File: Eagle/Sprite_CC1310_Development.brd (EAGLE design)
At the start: 50 x 50 mm, 68 parts

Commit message: Fixed HDMI
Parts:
- removed U$1: HDMID, HDMID:HDMID
- added R14, R16: 0, SparkFun:0603-RES
- added U$9: HDMID, HDMID:HDMID
- moved L3 3.45 mm to (31.7, 4.99), turned to 180 degrees
- moved R15 3.02 mm to (30.5, 7.67), turned to 90 degrees
- moved C23 0.71 mm to (44.8, 22.9), turned to 270 degrees
- moved R21 0.27 mm to (21.8, 19.3)
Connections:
- new net N$16: R16.2, U$7.SIG
- new net N$40: R14.1, U$3.SIG
- net GND: now also U$9.1, U$9.FOOT1, U$9.FOOT2, U$9.FOOT3, U$9.FOOT4; no longer U$1.19, U$1.FOOT1, U$1.FOOT2, U$1.FOOT3, U$1.FOOT4
- net JTAG_TCKC: now also U$9.14, U$9.15; no longer U$1.5, U$1.6
- net JTAG_TMSC: now also U$9.16, U$9.17; no longer U$1.3, U$1.4
- net N$14: now also R16.1; no longer U$7.SIG
- net N$26: now also R14.2; no longer U$3.SIG
- net RESET: now also U$9.6, U$9.7; no longer U$1.13, U$1.14
- net RXD: now also U$9.2, U$9.3; no longer U$1.17, U$1.18
- net SWO: now also U$9.8, U$9.9; no longer U$1.11, U$1.12
- net TDI: now also U$9.10, U$9.11; no longer U$1.10, U$1.9
- net TDO: now also U$9.12, U$9.13; no longer U$1.7, U$1.8
- net TXD: now also U$9.4, U$9.5; no longer U$1.15, U$1.16
- net VDDS: now also U$9.18, U$9.19; no longer U$1.1, U$1.2
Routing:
- net VDDS: track 124.6 -> 118.5 mm
- net GND: track 210.1 -> 204.6 mm, vias 13 -> 12
- net SWO: track 16.7 -> 12.6 mm
- net JTAG_TCKC: track 16.7 -> 12.8 mm
- net RESET: track 16.3 -> 12.4 mm
- net TDO: track 16.7 -> 12.7 mm
- net JTAG_TMSC: track 17.4 -> 13.4 mm
- net TDI: track 16.6 -> 12.7 mm
- net TXD: track 41.9 -> 38.2 mm
- net RXD: track 49.7 -> 46.0 mm
- net N$40: track 0.00 -> 3.35 mm
- net N$15: track 15.6 -> 12.8 mm
- net N$16: track 0.00 -> 2.21 mm
- net N$26: track 8.69 -> 7.47 mm

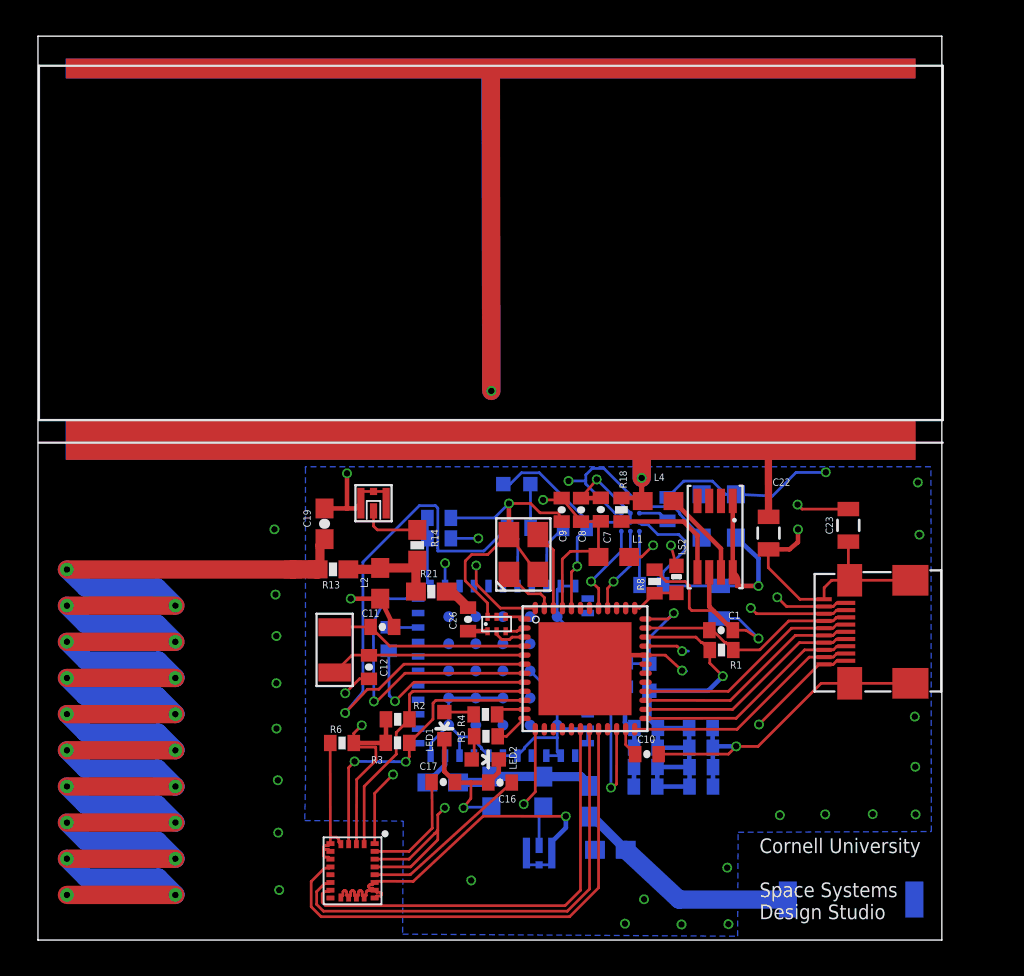
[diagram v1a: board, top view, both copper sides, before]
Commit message: updated boost converter, eliminated unnecessary tuning components, rotated oscillator, updated solar pads
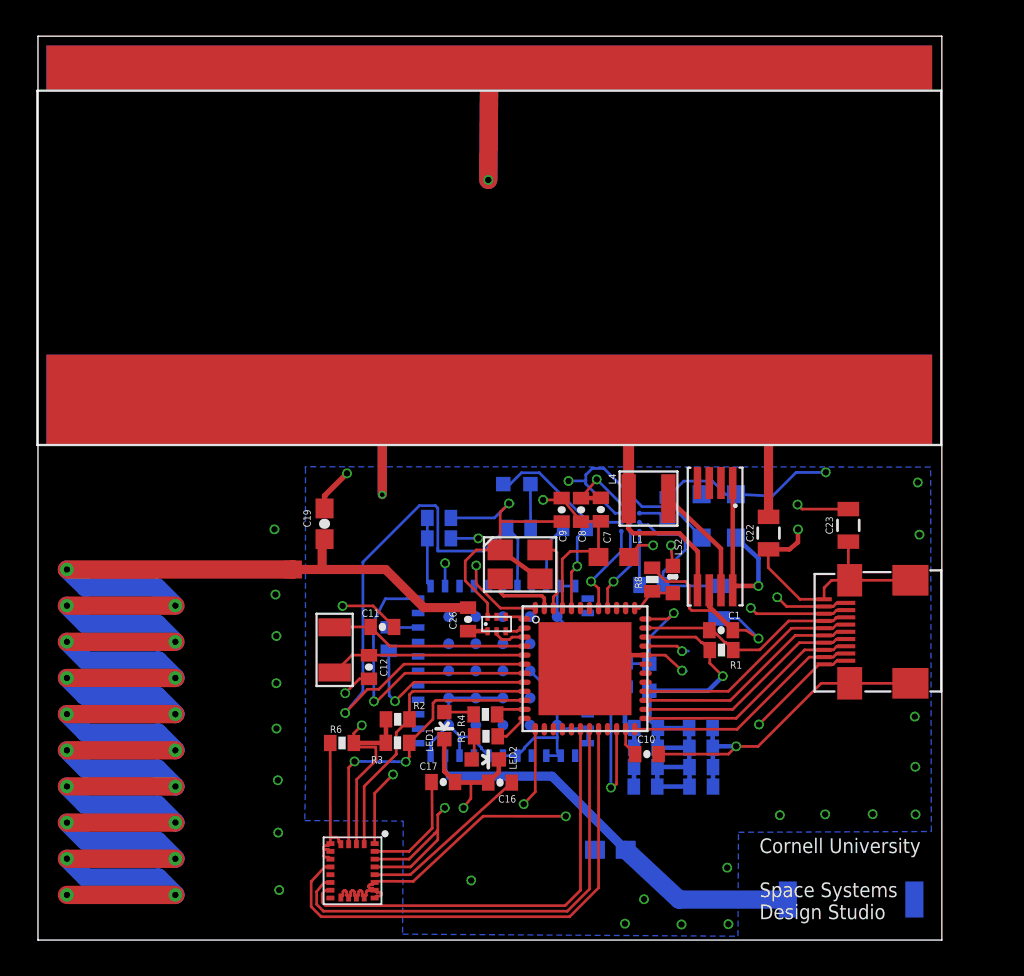
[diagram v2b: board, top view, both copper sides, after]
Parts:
- removed L2: DNP, SparkFun:0603
- removed R13, R14, R15, R16, R21, R22: 0, SparkFun:0603-RES
- removed R17: DNP, SparkFun:0603-RES
- removed R18: 10k, SparkFun:0402-RES
- removed U$3, U$7: MM5329-2700, MM5329-2700:MM5829-2700
- L4: value 47uH -> 10uH; device SparkFun:0603 -> ASPI-0315FS:ASPI-0315FS
- moved FRONT_PANEL 1.39 mm to (25.0, 37.2)
- moved REAR_PANEL 1.38 mm to (25.0, 37.2)
- moved TSX3225 0.58 mm to (26.7, 20.8), turned to 0 degrees
- moved L4 0.55 mm to (33.8, 24.4)
- moved LS2 0.20 mm to (35.1, 19.9)
- moved R8 0.17 mm to (34.0, 19.9)
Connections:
- removed net N$14: R15.2, R16.1, R17.1, R22.1
- removed net N$16: R16.2, U$7.SIG
- removed net N$25: GPS.32, R22.2
- removed net N$26: L2.1, R13.1, R14.2, R21.2
- removed net N$27: C26.1, R21.1
- removed net N$40: R14.1, U$3.SIG
- removed net N$41: R18.1, U$8.5
- net ANTENNA: now also C26.1; no longer R13.2
- net GND: no longer L2.2, R17.2, U$3.GND1, U$3.GND2, U$3.GND3, U$7.GND1, U$7.GND2, U$7.GND3
- net N$15: now also GPS.32; no longer R15.1
- net SOLAR_CELLS: now also U$8.5; no longer R18.2
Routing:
- net GND: track 204.6 -> 181.2 mm
- net SOLAR_CELLS: track 35.4 -> 50.1 mm
- net N$15: track 12.8 -> 22.7 mm
- net ANTENNA: track 131.2 -> 140.3 mm
- net N$14: track 7.66 -> 0.00 mm
- net N$26: track 7.47 -> 0.00 mm
- net N$41: track 6.57 -> 0.00 mm
- net N$40: track 3.35 -> 0.00 mm
- net N$16: track 2.21 -> 0.00 mm
- net N$25: track 1.89 -> 0.00 mm
- net N$27: track 1.55 -> 0.00 mm
- net VDDS: track 118.5 -> 120.0 mm
- net N$48: track 5.03 -> 6.32 mm
- net X24M_P: track 3.08 -> 3.87 mm

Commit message: still need to add breakouts
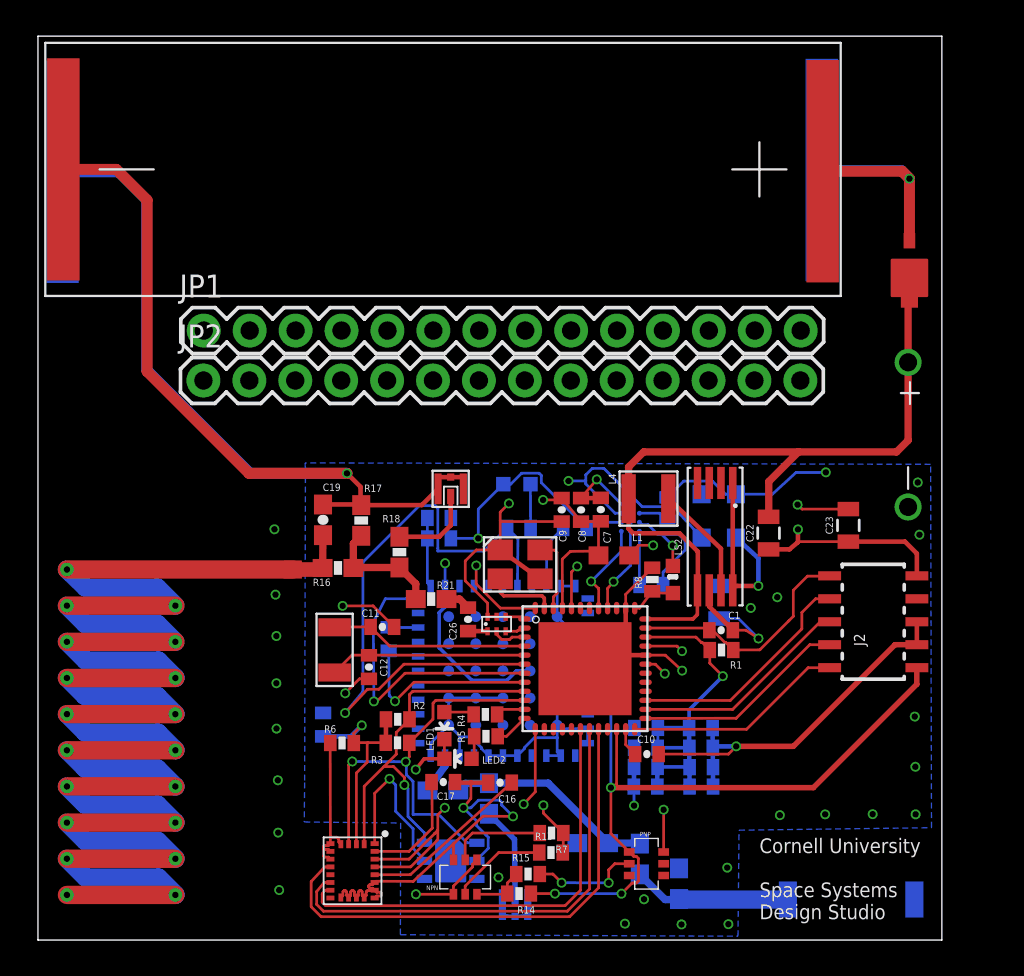
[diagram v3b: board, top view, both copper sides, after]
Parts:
- removed LS1: LIGHTSENSORALS, SparkFun-Sensors:ALS-PT19
- removed U$9: HDMID, HDMID:HDMID
- added C21: 0.1 uF, SparkFun:0402-CAP
- added J2: CORTEX_DEBUG_SMD, SparkFun-Connectors:SAMTECH_FTSH-105-01
- added JP1, JP2: (no value), SparkFun-Connectors:1X14
- added NPN: MMDT3904, mmdt3904:MMDT3904
- added PNP: MMDT3906, mmdt3906:MMDT3906
- added R13, R15: 330, SparkFun:0402-RES
- added R14: 10k, SparkFun:0402-RES
- added R16, R21, R22, R23: 0, SparkFun:0603-RES
- added R17, R18, R24, R25: DNP, SparkFun:0603-RES
- added SCHTOKKY: STPS1L30MF, stps1l30mf:STPS1L30MF
- added SI7021: SI7021, si7021:SI7021
- added SUPERCAPACITOR: SUPERCAP1, supercap1:SUPERCAP1
- added U$1, U$3: MM5329-2700, MM5329-2700:MM5829-2700
- FRONT_PANEL, REAR_PANEL: value ALTA_CELL -> SOLARMD; device ALTA_CELL:ALTA_CELL -> solarmd:SOLARMD
- R20: value 331 -> 330
- R7: value 10k -> 330
- moved R7 9.64 mm to (28.4, 5.92), flipped to the top, turned to 180 degrees
- moved FRONT_PANEL 6.02 mm to (22.4, 42.6), flipped to the top, turned to 0 degrees
- moved REAR_PANEL 5.92 mm to (22.4, 42.5), flipped to the bottom
- moved L3 4.24 mm to (35.5, 3.12), turned to 270 degrees
- moved LED2 1.51 mm to (23.2, 10.0), turned to 90 degrees
- moved C19 0.24 mm to (15.8, 23.2)
- moved L1 0.09 mm to (31.9, 21.3)
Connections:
- removed net ADC0: LS1.E, MICROCONTROLLER.36, R7.1
- new net BPNP: NPN.6, R14.2, R15.1
- new net IMUGND: C13.2, C14.2, C15.2, C16.2, C17.2, IMU.14, IMU.15, IMU.16, IMU.17, IMU.18, IMU.19, IMU.20, NPN.3, SI7021.2
- new net N$14: NPN.2, R7.2
- new net N$16: NPN.5, R13.1
- new net N$25: PNP.2, R15.2
- new net N$26: R16.2, R17.1, R18.2, R21.1
- new net N$27: C26.1, R21.2
- new net N$40: R18.1, U$1.SIG
- new net N$41: GPS.32, R22.1
- new net N$49: R22.2, R23.1, R24.1, R25.1
- new net N$50: R25.2, U$3.SIG
- new net SUPERCAP: C22.1, L4.2, MICROCONTROLLER.36, SCHTOKKY.-, SUPERCAPACITOR.+, U$8.5
- new net TRANS: MICROCONTROLLER.31, R13.2, R7.1
- new net VSENSE: GPS.2, GPS.58, LED3.A, LS2.C, PNP.6, R11.2, R12.1, R19.2, U$2.VCC, U$2.VM
- net ANTENNA: now also R16.1; no longer C26.1
- net GND: now also C21.2, J2.3, J2.5, J2.9, MICROCONTROLLER.38, NPN.1, NPN.4, R17.2, R24.2, SUPERCAPACITOR.-, U$1.GND1, U$1.GND2, U$1.GND3, U$3.GND1, U$3.GND2, U$3.GND3; no longer C13.2, C14.2, C15.2, C16.2, C17.2, IMU.14, IMU.15, IMU.16, IMU.17, IMU.18, IMU.19, IMU.20, R7.2, U$9.1, U$9.FOOT1, U$9.FOOT2, U$9.FOOT3, U$9.FOOT4
- net JTAG_TCKC: now also J2.4; no longer U$9.14, U$9.15
- net JTAG_TMSC: now also J2.2; no longer U$9.16, U$9.17
- net N$15: now also R23.2; no longer GPS.32
- net RESET: now also J2.10; no longer U$9.6, U$9.7
- net RXD: no longer U$9.2, U$9.3
- net SCL: now also SI7021.6
- net SDA: now also SI7021.1
- net SOLAR_CELLS: now also SCHTOKKY.+; no longer C22.1, L4.2, U$8.5
- net SWO: no longer U$9.8, U$9.9
- net TDI: now also J2.8; no longer U$9.10, U$9.11
- net TDO: now also J2.6; no longer U$9.12, U$9.13
- net TXD: no longer U$9.4, U$9.5
- net VDDS: now also C21.1, J2.1, PNP.1, R14.1, SI7021.5; no longer GPS.2, GPS.58, LED3.A, LS1.C, LS2.C, R11.2, R12.1, R19.2, U$2.VCC, U$2.VM, U$9.18, U$9.19
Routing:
- net VSENSE: track 0.00 -> 64.3 mm, vias 0 -> 4
- net SUPERCAP: track 0.00 -> 42.3 mm
- net IMUGND: track 0.00 -> 37.0 mm, vias 0 -> 3
- net SOLAR_CELLS: track 50.1 -> 13.5 mm
- net TRANS: track 0.00 -> 14.6 mm, vias 0 -> 2
- net N$15: track 22.7 -> 8.79 mm
- net SWO: track 12.6 -> 0.00 mm
- net N$49: track 0.00 -> 11.6 mm
- net ANTENNA: track 140.3 -> 131.5 mm
- net SDA: track 16.6 -> 23.8 mm
- net ADC0: track 6.77 -> 0.00 mm, vias 1 -> 0
- net N$26: track 0.00 -> 6.64 mm
- net N$25: track 0.00 -> 6.01 mm, vias 0 -> 2
- net GND: track 181.2 -> 187.2 mm, vias 12 -> 11
- net TXD: track 38.2 -> 32.7 mm
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
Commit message: board layout complete, need to update other files
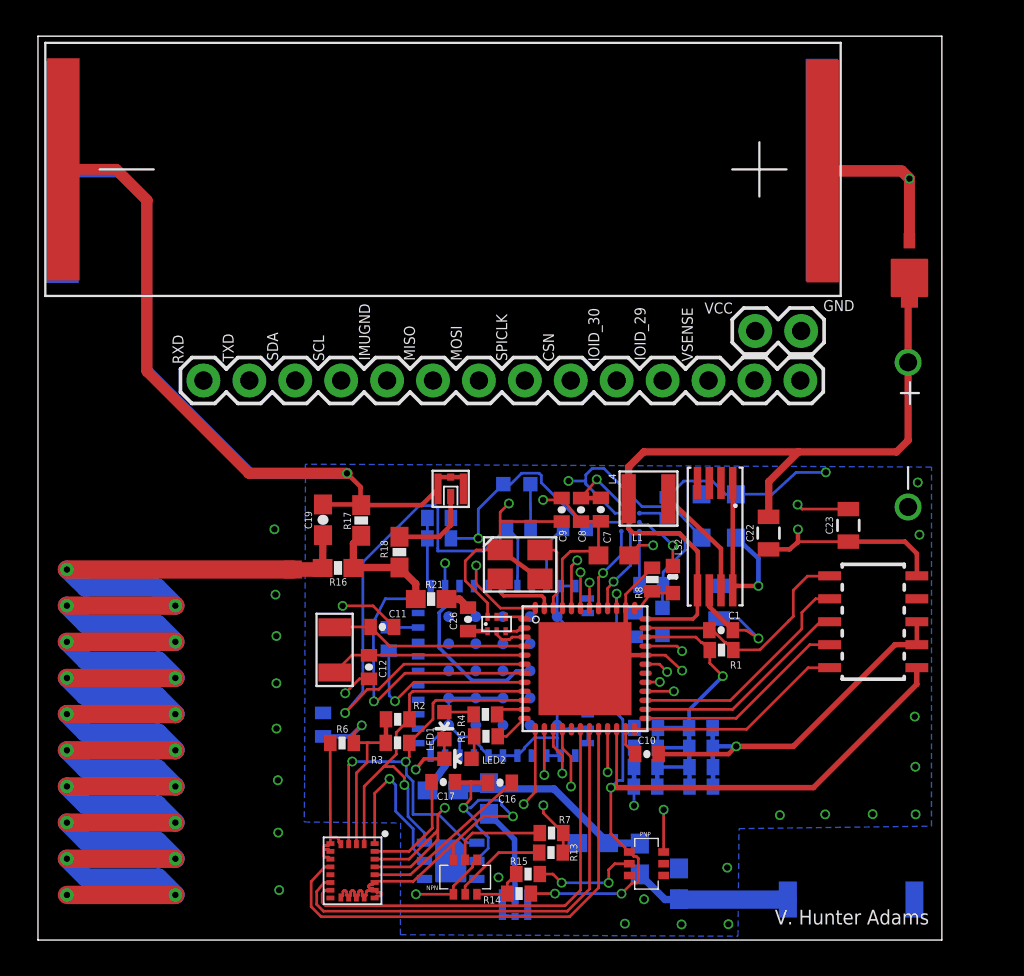
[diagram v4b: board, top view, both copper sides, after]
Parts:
- added LS1: LIGHTSENSORALS, SparkFun-Sensors:ALS-PT19
- added R26: 10k, SparkFun:0402-RES
- JP1: device SparkFun-Connectors:1X14 -> SparkFun:1X02
- moved JP1 30.5 mm to (39.7, 33.7)
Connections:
- removed net SWO: MICROCONTROLLER.28
- new net ADC2: LS1.E, MICROCONTROLLER.39, R26.1
- new net CSN: JP2.9, MICROCONTROLLER.21
- new net CTS: JP2.13, MICROCONTROLLER.29
- new net DIO_29: JP2.11, MICROCONTROLLER.42
- new net DIO_30: JP2.10, MICROCONTROLLER.43
- new net MISO: JP2.6, MICROCONTROLLER.14
- new net MOSI: JP2.7, MICROCONTROLLER.15
- new net RTS: JP2.14, MICROCONTROLLER.28
- new net SPICLK: JP2.8, MICROCONTROLLER.16
- net GND: now also JP1.2, R26.2
- net IMUGND: now also JP2.5
- net RXD: now also JP2.1
- net SCL: now also JP2.4
- net SDA: now also JP2.3
- net TXD: now also JP2.2
- net VDDS: now also JP1.1
- net VSENSE: now also JP2.12, LS1.C
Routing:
- net MOSI: track 0.00 -> 27.2 mm, vias 0 -> 1
- net MISO: track 0.00 -> 27.0 mm, vias 0 -> 1
- net SPICLK: track 0.00 -> 26.9 mm, vias 0 -> 1
- net CSN: track 0.00 -> 25.4 mm, vias 0 -> 1
- net IMUGND: track 37.0 -> 62.4 mm
- net SCL: track 21.2 -> 46.2 mm
- net SDA: track 23.8 -> 47.5 mm
- net RTS: track 0.00 -> 21.7 mm, vias 0 -> 1
- net CTS: track 0.00 -> 20.3 mm, vias 0 -> 1
- net DIO_29: track 0.00 -> 14.4 mm, vias 0 -> 1
- net DIO_30: track 0.00 -> 13.6 mm, vias 0 -> 1
- net VSENSE: track 64.3 -> 75.5 mm
- net ADC2: track 0.00 -> 5.66 mm, vias 0 -> 1
- net TRANS: track 14.6 -> 18.3 mm
- net RXD: track 41.9 -> 38.6 mm, vias 2 -> 1
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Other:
- board text added: "CSN"
- board text added: "GND"
- board text added: "IMUGND"
- board text added: "IOID_29"
- board text added: "IOID_30"
- board text added: "MISO"
- board text added: "MOSI"
- board text added: "RXD"
- board text added: "SCL"
- board text added: "SDA"
- board text added: "SPICLK"
- board text added: "TXD"
- board text added: "V. Hunter Adams"
- board text added: "VCC"
- board text added: "VSENSE"
- board text removed: "Cornell University Space Systems Design Studio"
- board text removed: "V. Hunter Adams VHA3@CORNELL.EDU"

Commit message: updated all files
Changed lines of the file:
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@@
 <setting verticaltext="up"/>
 </settings>
-<grid distance="0.002" unitdist="inch" unit="inch" style="lines" multiple="1" display="yes" altdistance="0.000123031496" altunitdist="mil" altunit="mil"/>
+<grid distance="0.002" unitdist="inch" unit="mm" style="lines" multiple="1" display="yes" altdistance="0.000003125" altunitdist="mm" altunit="mm"/>
 <layers>
-<layer number="1" name="Top" color="4" fill="1" visible="no" active="yes"/>
-<layer number="2" name="Route2" color="1" fill="3" visible="no" active="yes"/>
+<layer number="1" name="Top" color="4" fill="1" visible="yes" active="yes"/>
+<layer number="2" name="Route2" color="1" fill="3" visible="yes" active="yes"/>
 <layer number="3" name="Route3" color="4" fill="3" visible="no" active="yes"/>
 <layer number="4" name="Route4" color="1" fill="4" visible="no" active="yes"/>
@@
 <layer number="13" name="Route13" color="4" fill="5" visible="no" active="yes"/>
 <layer number="14" name="Route14" color="1" fill="6" visible="no" active="yes"/>
-<layer number="15" name="Route15" color="4" fill="6" visible="no" active="yes"/>
-<layer number="16" name="Bottom" color="1" fill="1" visible="yes" active="yes"/>
+<layer number="15" name="Route15" color="4" fill="6" visible="yes" active="yes"/>
+<layer number="16" name="Bottom" color="1" fill="1" visible="no" active="yes"/>
 <layer number="17" name="Pads" color="2" fill="1" visible="yes" active="yes"/>
 <layer number="18" name="Vias" color="2" fill="1" visible="yes" active="yes"/>
 <layer number="19" name="Unrouted" color="6" fill="1" visible="yes" active="yes"/>
 <layer number="20" name="Dimension" color="24" fill="1" visible="yes" active="yes"/>
-<layer number="21" name="tPlace" color="7" fill="1" visible="no" active="yes"/>
-<layer number="22" name="bPlace" color="7" fill="1" visible="yes" active="yes"/>
-<layer number="23" name="tOrigins" color="15" fill="1" visible="no" active="yes"/>
-<layer number="24" name="bOrigins" color="15" fill="1" visible="yes" active="yes"/>
-<layer number="25" name="tNames" color="7" fill="1" visible="no" active="yes"/>
-<layer number="26" name="bNames" color="7" fill="1" visible="yes" active="yes"/>
+<layer number="21" name="tPlace" color="7" fill="1" visible="yes" active="yes"/>
+<layer number="22" name="bPlace" color="7" fill="1" visible="no" active="yes"/>
+<layer number="23" name="tOrigins" color="15" fill="1" visible="yes" active="yes"/>
+<layer number="24" name="bOrigins" color="15" fill="1" visible="no" active="yes"/>
+<layer number="25" name="tNames" color="7" fill="1" visible="yes" active="yes"/>
+<layer number="26" name="bNames" color="7" fill="1" visible="no" active="yes"/>
 <layer number="27" name="tValues" color="7" fill="1" visible="no" active="yes"/>
-<layer number="28" name="bValues" color="7" fill="1" visible="yes" active="yes"/>
+<layer number="28" name="bValues" color="7" fill="1" visible="no" active="yes"/>
 <layer number="29" name="tStop" color="7" fill="3" visible="no" active="yes"/>
 <layer number="30" name="bStop" color="7" fill="6" visible="no" active="yes"/>
@@
 <layer number="43" name="vRestrict" color="2" fill="10" visible="no" active="yes"/>
 <layer number="44" name="Drills" color="7" fill="1" visible="no" active="yes"/>
-<layer number="45" name="Holes" color="7" fill="1" visible="no" active="yes"/>
+<layer number="45" name="Holes" color="7" fill="1" visible="yes" active="yes"/>
 <layer number="46" name="Milling" color="3" fill="1" visible="no" active="yes"/>
 <layer number="47" name="Measures" color="7" fill="1" visible="no" active="yes"/>
@@
 <text x="33.609421875" y="32.0637625" size="0.6096" layer="25" rot="R90">IOID_29</text>
 <text x="36.2235625" y="32.002575" size="0.6096" layer="25" rot="R90">VSENSE</text>
-<text x="36.866678125" y="34.6548125" size="0.6096" layer="25">VCC</text>
-<text x="43.439403125" y="34.791646875" size="0.6096" layer="25">GND</text>
+<text x="38.0907875" y="32.955078125" size="0.6096" layer="25" rot="R90">VCC</text>
+<text x="44.354753125" y="32.873003125" size="0.6096" layer="25" rot="R90">GND</text>
+<hole x="47" y="47" drill="4"/>
 </plain>
 <attributes>
